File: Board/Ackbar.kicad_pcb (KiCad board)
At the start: 2 copper layers, 101.6 x 50.8 mm, 15 parts, among them J1 TOF, J2 GNSS, J3 HALL, J4 MOTOR, J5 PWR_IN, J6 EPD, U1 ESP32-S3 Pico, U2 VREG, U3 TMC2209

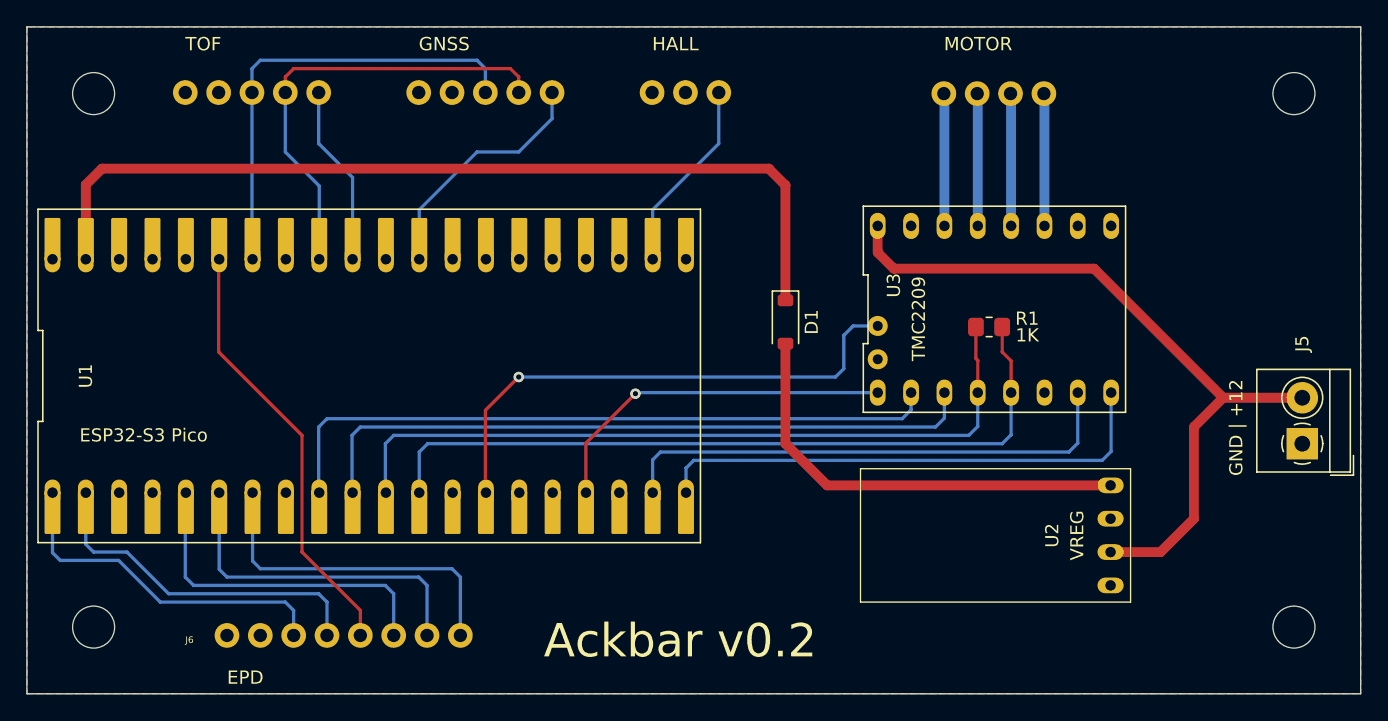
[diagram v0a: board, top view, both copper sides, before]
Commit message: Add delay time
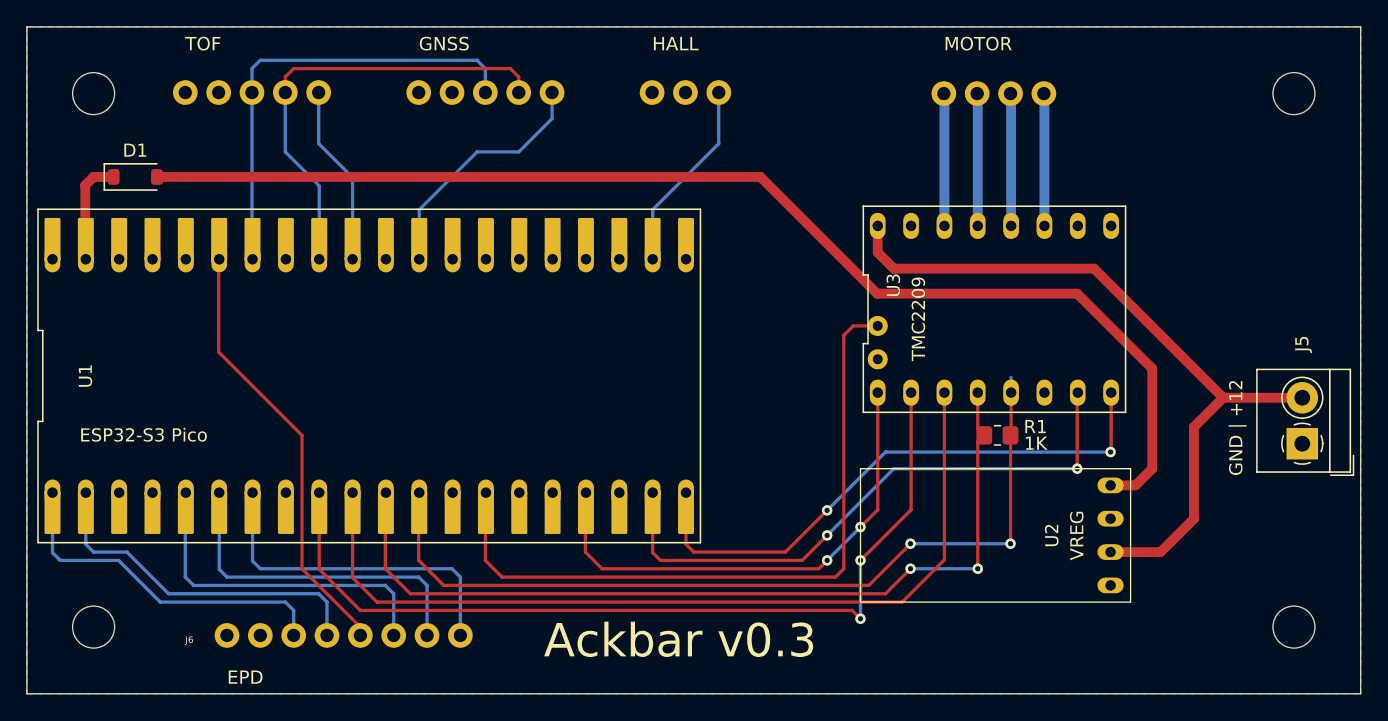
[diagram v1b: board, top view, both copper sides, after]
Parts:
- moved D1 50.7 mm to (21.0, 24.1), turned to 0 degrees
- moved R1 8.28 mm to (86.6, 43.8)
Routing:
- net /VSYS: track 68.8 -> 8.08 mm
- net /VOUT: track 33.7 -> 93.2 mm
- net /STP_MS1: track 51.9 -> 67.5 mm, vias 0 -> 2
- net /STP_MS2: track 51.9 -> 66.4 mm
- net /STP_DIAG: track 40.3 -> 53.9 mm, vias 1 -> 0
- net /STP_EN: track 27.6 -> 38.1 mm, vias 1 -> 2
- net /STP_MS3: track 57.0 -> 66.3 mm, vias 0 -> 2
- net /STP_PDN: track 57.2 -> 65.1 mm, vias 0 -> 2
- net /STP_STEP: track 39.3 -> 45.9 mm, vias 0 -> 2
- net /STP_DIR: track 39.3 -> 44.2 mm, vias 0 -> 2
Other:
- board text added: "Ackbar v0.3"
- board text removed: "Ackbar v0.2"

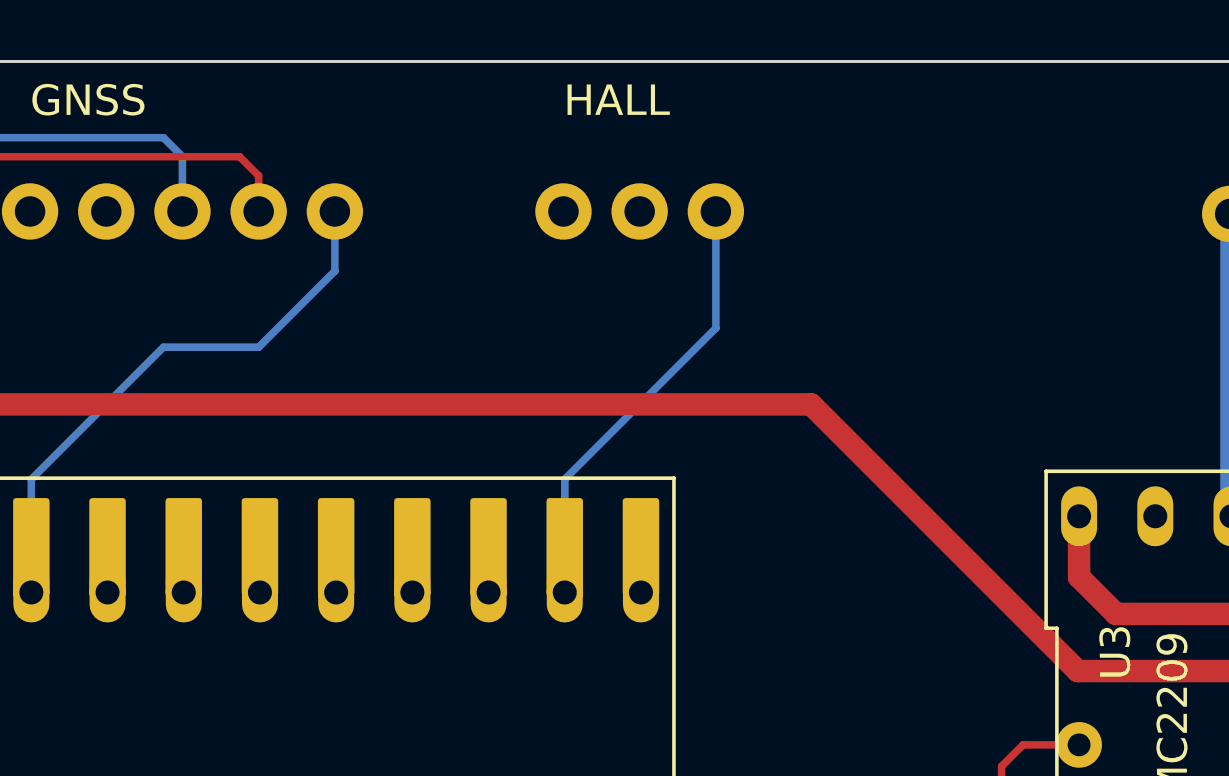
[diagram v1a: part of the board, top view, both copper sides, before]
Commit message: Break out a few currently unused pins for config jumpers
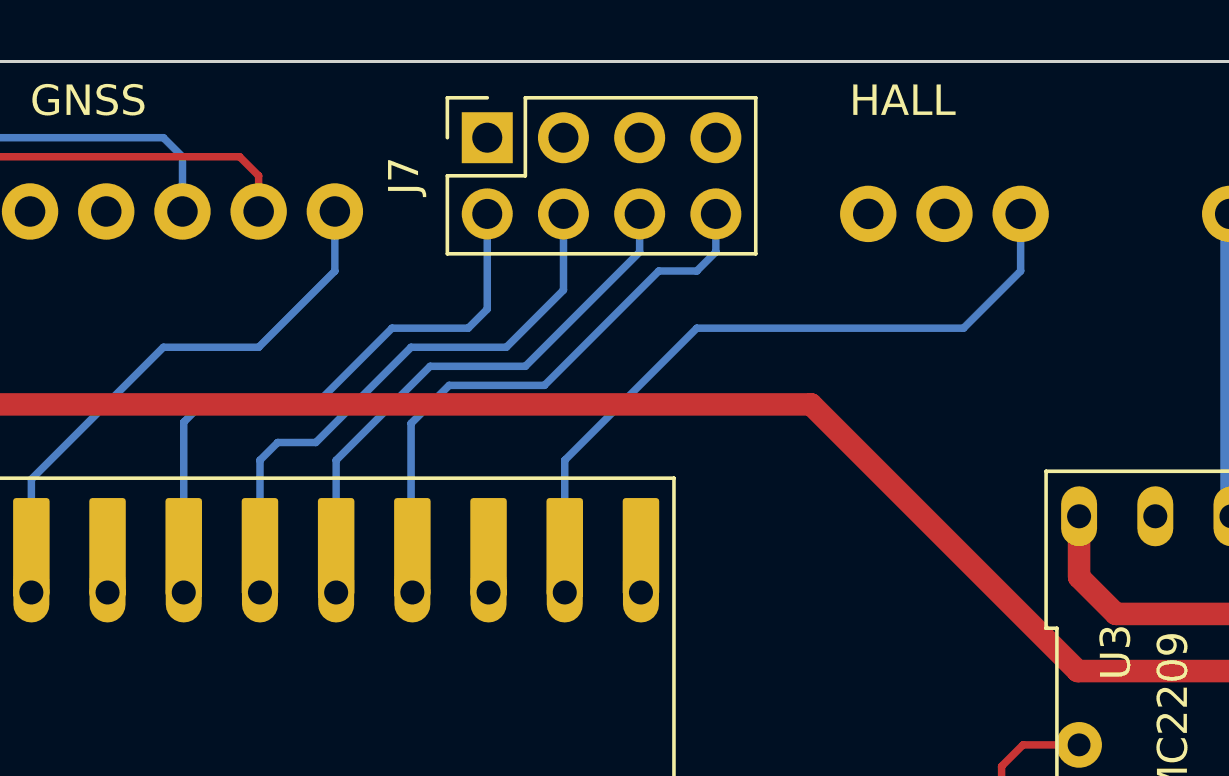
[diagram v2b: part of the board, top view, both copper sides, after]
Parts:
- added J7: Conn_02x04_Odd_Even, Connector_PinSocket_2.54mm:PinSocket_2x04_P2.54mm_Vertical, F.Cu at (57.8, 15.2)
- moved J3 10.2 mm to (70.5, 17.8)
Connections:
- U1 pad 24: unconnected-(U1-GP1-Pad24) -> Net-(J7-Pin_8)
- U1 pad 25: unconnected-(U1-GP2-Pad25) -> Net-(J7-Pin_6)
- U1 pad 26: unconnected-(U1-GP4-Pad26) -> Net-(J7-Pin_4)
- U1 pad 27: unconnected-(U1-GP5-Pad27) -> Net-(J7-Pin_2)
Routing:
- net Net-(J7-Pin_2): track 0.00 -> 20.5 mm
- net Net-(J7-Pin_8): track 0.00 -> 19.4 mm
- net Net-(J7-Pin_4): track 0.00 -> 19.4 mm
- net Net-(J7-Pin_6): track 0.00 -> 18.7 mm
- net /HALL: track 14.8 -> 24.1 mm
